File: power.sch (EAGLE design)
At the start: 36 parts, among them IC1 74HC125D, IC2 7805TV, IC3 7815TV

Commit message: fixed more things that had been bothering me.
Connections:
- net GND: now also U$3.P$3; no longer U$3.P$4
- net N$1: now also U$3.P$2, U$4.P$1, U$5.P$2; no longer D1.A, U$3.P$3
- net N$3: now also D1.A, U$3.P$4; no longer IC3.VI, PV+.MOUNT, R3.1, U$3.P$2
- net N$6: now also IC3.VI, PV+.MOUNT, R3.1; no longer U$4.P$1, U$5.P$2
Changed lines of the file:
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@@
 </busses>
 <nets>
-<net name="N$3" class="0">
-<segment>
-<pinref part="R3" gate="G$1" pin="1"/>
-<wire x1="7.62" y1="43.18" x2="2.54" y2="43.18" width="0.1524" layer="91"/>
-<wire x1="7.62" y1="43.18" x2="7.62" y2="40.64" width="0.1524" layer="91"/>
-<wire x1="7.62" y1="40.64" x2="7.62" y2="33.02" width="0.1524" layer="91"/>
-<wire x1="7.62" y1="33.02" x2="2.54" y2="33.02" width="0.1524" layer="91"/>
-<wire x1="7.62" y1="40.64" x2="22.86" y2="40.64" width="0.1524" layer="91"/>
-<junction x="7.62" y="40.64"/>
-<pinref part="U$3" gate="G$1" pin="P$2"/>
-<wire x1="22.86" y1="40.64" x2="22.86" y2="43.18" width="0.1524" layer="91"/>
-<pinref part="PV+" gate="G$1" pin="MOUNT"/>
-<pinref part="IC3" gate="A1" pin="VI"/>
-<wire x1="-58.42" y1="76.2" x2="-60.96" y2="76.2" width="0.1524" layer="91"/>
-<wire x1="-60.96" y1="76.2" x2="-60.96" y2="50.8" width="0.1524" layer="91"/>
-<wire x1="-60.96" y1="50.8" x2="2.54" y2="50.8" width="0.1524" layer="91"/>
-<wire x1="2.54" y1="50.8" x2="2.54" y2="43.18" width="0.1524" layer="91"/>
-<junction x="2.54" y="43.18"/>
-</segment>
-</net>
 <net name="N$9" class="0">
 <segment>
@@
 </segment>
 </net>
-<net name="N$1" class="0">
-<segment>
-<pinref part="D1" gate="1" pin="A"/>
-<pinref part="U$3" gate="G$1" pin="P$3"/>
-<wire x1="55.88" y1="76.2" x2="12.7" y2="76.2" width="0.1524" layer="91"/>
-<wire x1="12.7" y1="76.2" x2="12.7" y2="60.96" width="0.1524" layer="91"/>
-</segment>
-</net>
 <net name="N$2" class="0">
 <segment>
@@
 </segment>
 </net>
-<net name="N$6" class="0">
-<segment>
-<pinref part="U$5" gate="G$1" pin="P$2"/>
-<wire x1="30.48" y1="55.88" x2="27.94" y2="55.88" width="0.1524" layer="91"/>
-<wire x1="27.94" y1="55.88" x2="27.94" y2="45.72" width="0.1524" layer="91"/>
-<pinref part="U$4" gate="G$1" pin="P$1"/>
-<wire x1="27.94" y1="45.72" x2="30.48" y2="45.72" width="0.1524" layer="91"/>
-<junction x="27.94" y="45.72"/>
-<wire x1="27.94" y1="45.72" x2="27.94" y2="38.1" width="0.1524" layer="91"/>
-<wire x1="27.94" y1="38.1" x2="12.7" y2="38.1" width="0.1524" layer="91"/>
-<pinref part="U$3" gate="G$1" pin="P$1"/>
-<wire x1="12.7" y1="38.1" x2="12.7" y2="43.18" width="0.1524" layer="91"/>
-</segment>
-</net>
 <net name="GND" class="0">
 <segment>
-<wire x1="22.86" y1="73.66" x2="50.8" y2="73.66" width="0.1524" layer="91"/>
+<wire x1="12.7" y1="73.66" x2="50.8" y2="73.66" width="0.1524" layer="91"/>
 <wire x1="50.8" y1="73.66" x2="50.8" y2="55.88" width="0.1524" layer="91"/>
 <wire x1="50.8" y1="55.88" x2="50.8" y2="50.8" width="0.1524" layer="91"/>
@@
 <pinref part="R1" gate="G$1" pin="1"/>
 <wire x1="73.66" y1="50.8" x2="78.74" y2="50.8" width="0.1524" layer="91"/>
-<pinref part="U$3" gate="G$1" pin="P$4"/>
-<wire x1="22.86" y1="73.66" x2="22.86" y2="60.96" width="0.1524" layer="91"/>
 <pinref part="U$5" gate="G$1" pin="P$4"/>
 <wire x1="48.26" y1="55.88" x2="50.8" y2="55.88" width="0.1524" layer="91"/>
@@
 <pinref part="GND1" gate="1" pin="GND"/>
 <junction x="60.96" y="50.8"/>
+<pinref part="U$3" gate="G$1" pin="P$3"/>
+<wire x1="12.7" y1="73.66" x2="12.7" y2="60.96" width="0.1524" layer="91"/>
 </segment>
 <segment>
@@
 </segment>
 </net>
+<net name="N$1" class="0">
+<segment>
+<pinref part="U$4" gate="G$1" pin="P$1"/>
+<pinref part="U$5" gate="G$1" pin="P$2"/>
+<wire x1="30.48" y1="55.88" x2="27.94" y2="55.88" width="0.1524" layer="91"/>
+<wire x1="27.94" y1="55.88" x2="27.94" y2="45.72" width="0.1524" layer="91"/>
+<wire x1="27.94" y1="45.72" x2="30.48" y2="45.72" width="0.1524" layer="91"/>
+<junction x="27.94" y="45.72"/>
+<wire x1="27.94" y1="45.72" x2="27.94" y2="38.1" width="0.1524" layer="91"/>
+<wire x1="27.94" y1="38.1" x2="22.86" y2="38.1" width="0.1524" layer="91"/>
+<pinref part="U$3" gate="G$1" pin="P$2"/>
+<wire x1="22.86" y1="43.18" x2="22.86" y2="38.1" width="0.1524" layer="91"/>
+</segment>
+</net>
+<net name="N$6" class="0">
+<segment>
+<pinref part="U$3" gate="G$1" pin="P$1"/>
+<wire x1="12.7" y1="38.1" x2="12.7" y2="43.18" width="0.1524" layer="91"/>
+<pinref part="R3" gate="G$1" pin="1"/>
+<wire x1="7.62" y1="43.18" x2="2.54" y2="43.18" width="0.1524" layer="91"/>
+<wire x1="7.62" y1="43.18" x2="7.62" y2="38.1" width="0.1524" layer="91"/>
+<wire x1="7.62" y1="38.1" x2="7.62" y2="33.02" width="0.1524" layer="91"/>
+<wire x1="7.62" y1="33.02" x2="2.54" y2="33.02" width="0.1524" layer="91"/>
+<pinref part="PV+" gate="G$1" pin="MOUNT"/>
+<pinref part="IC3" gate="A1" pin="VI"/>
+<wire x1="-58.42" y1="76.2" x2="-60.96" y2="76.2" width="0.1524" layer="91"/>
+<wire x1="-60.96" y1="76.2" x2="-60.96" y2="50.8" width="0.1524" layer="91"/>
+<wire x1="-60.96" y1="50.8" x2="2.54" y2="50.8" width="0.1524" layer="91"/>
+<wire x1="2.54" y1="50.8" x2="2.54" y2="43.18" width="0.1524" layer="91"/>
+<junction x="2.54" y="43.18"/>
+<wire x1="12.7" y1="38.1" x2="7.62" y2="38.1" width="0.1524" layer="91"/>
+<junction x="7.62" y="38.1"/>
+</segment>
+</net>
+<net name="N$3" class="0">
+<segment>
+<pinref part="D1" gate="1" pin="A"/>
+<wire x1="55.88" y1="76.2" x2="22.86" y2="76.2" width="0.1524" layer="91"/>
+<pinref part="U$3" gate="G$1" pin="P$4"/>
+<wire x1="22.86" y1="60.96" x2="22.86" y2="76.2" width="0.1524" layer="91"/>
+</segment>
+</net>

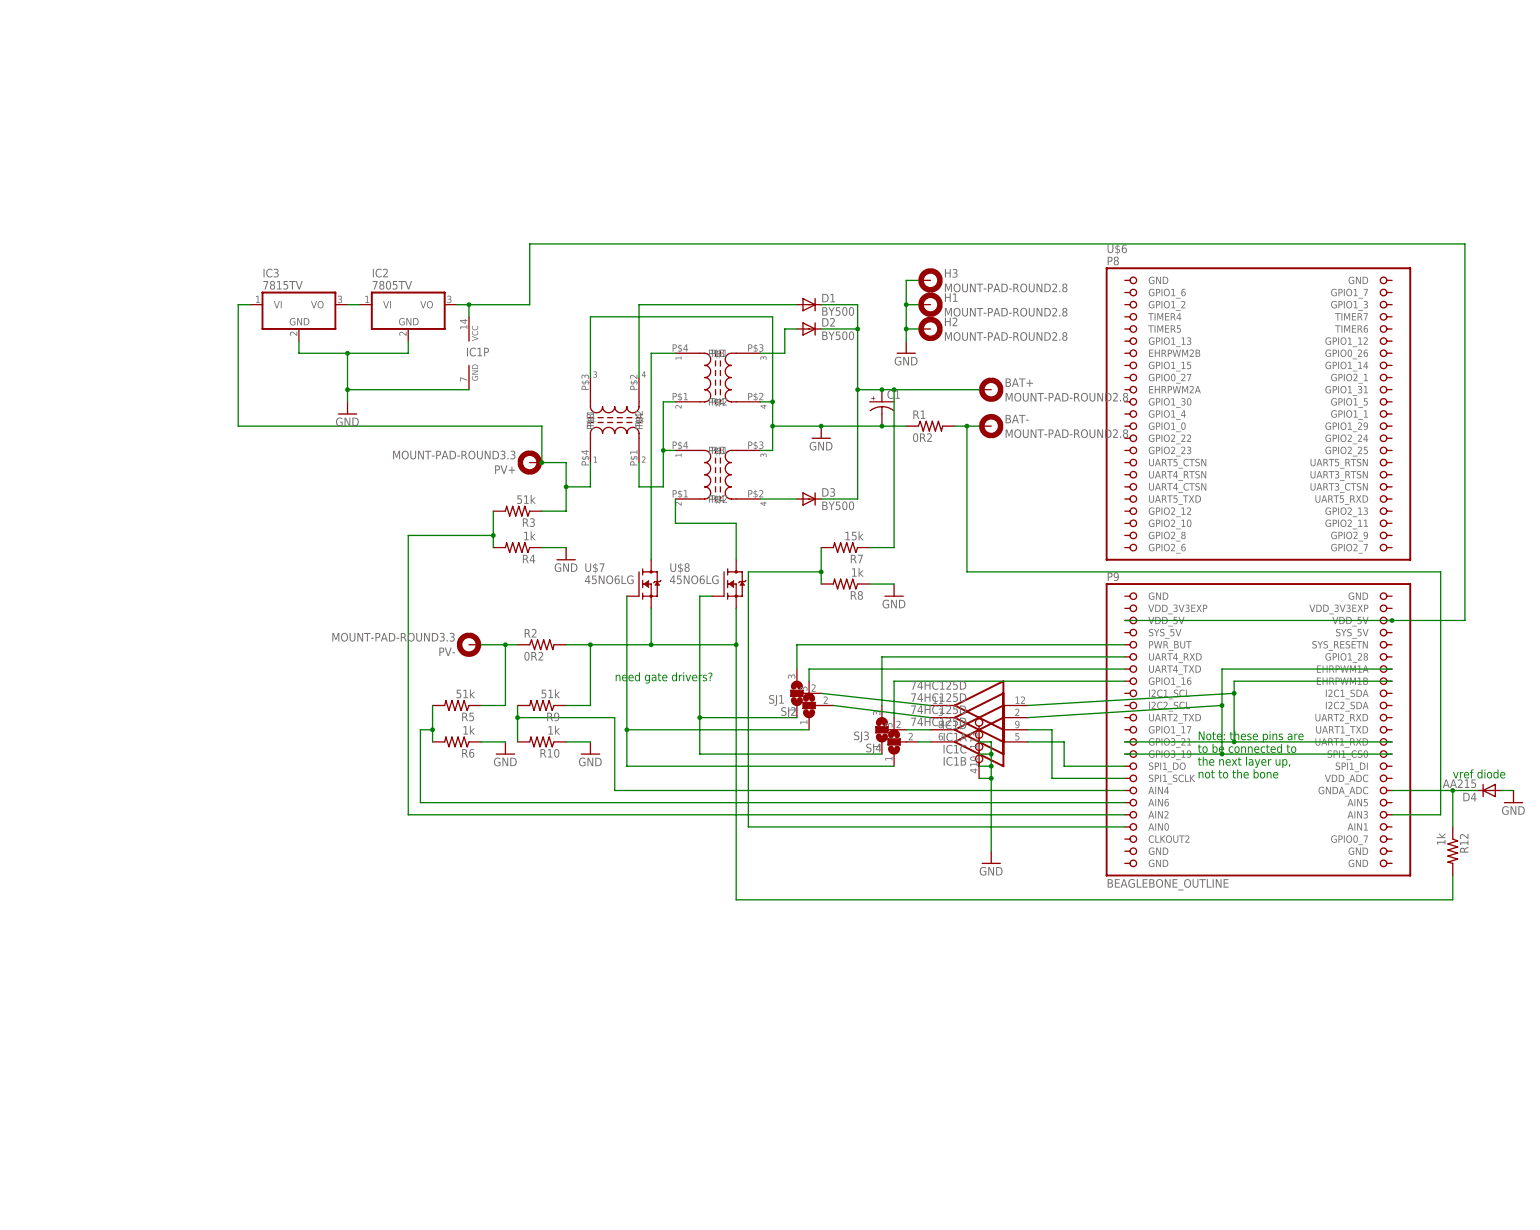
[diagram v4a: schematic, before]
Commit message: Schematic cleanup
Thanks, Roger!
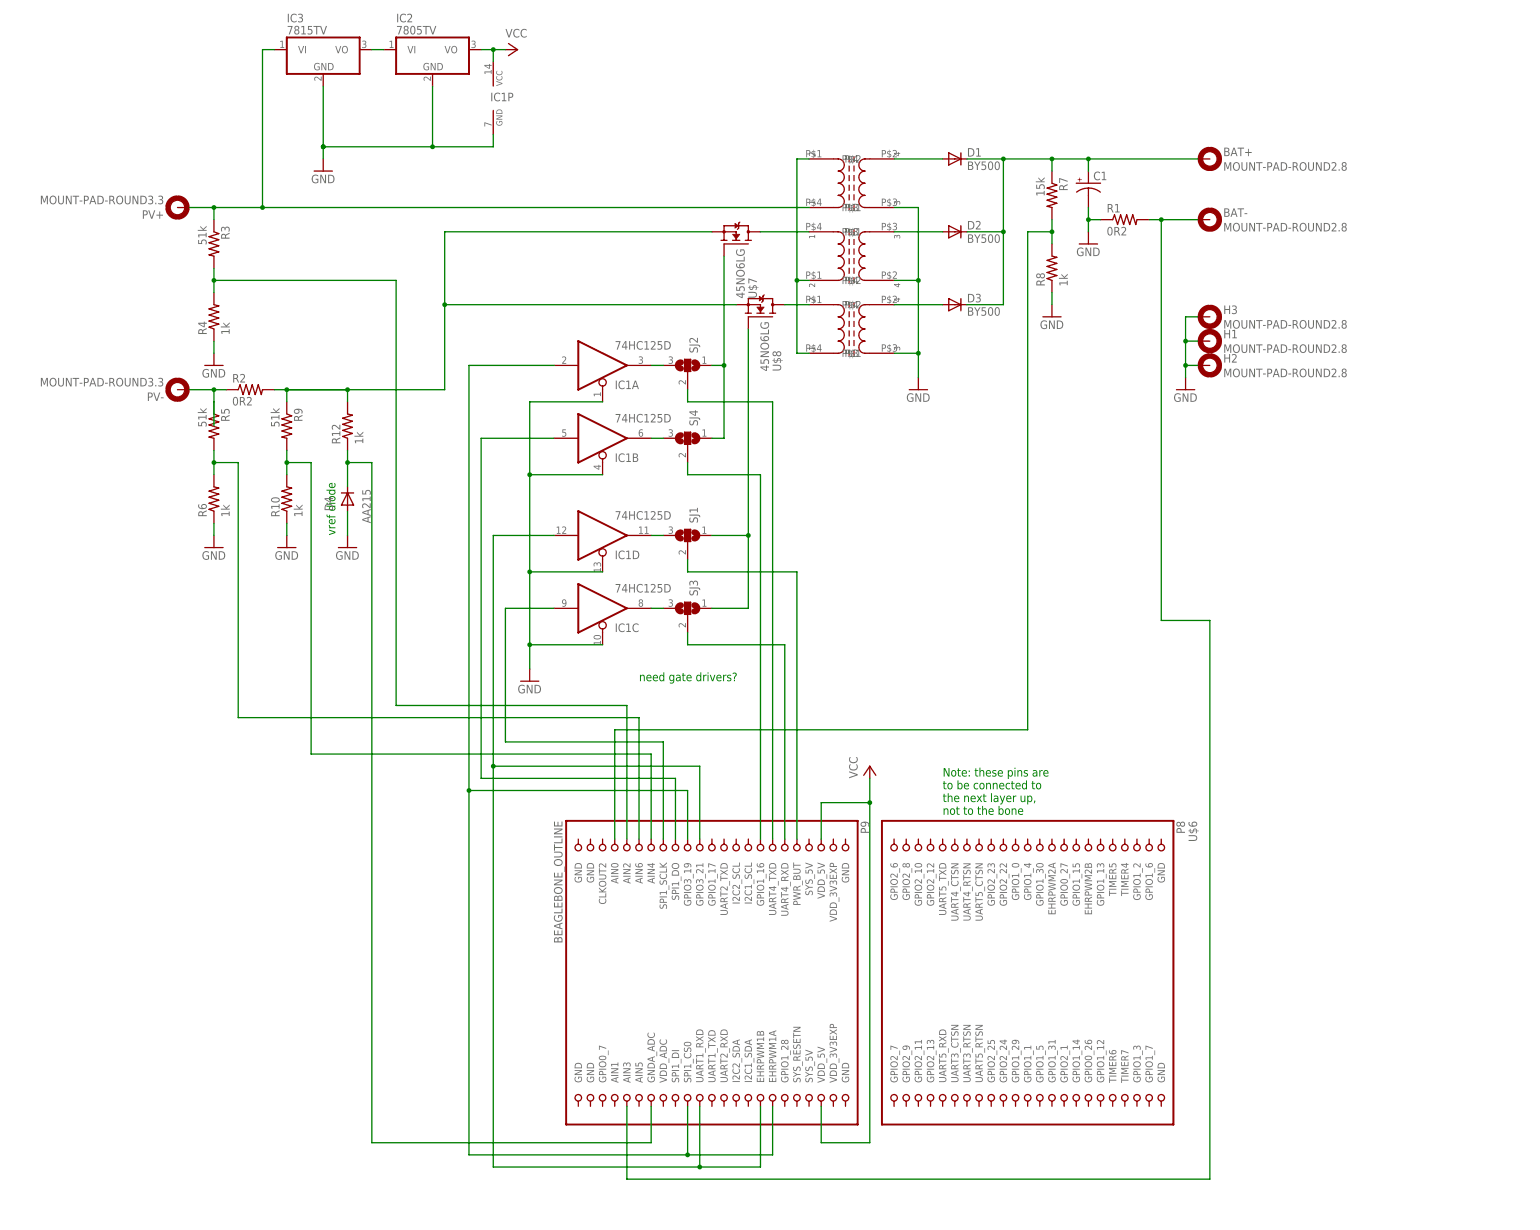
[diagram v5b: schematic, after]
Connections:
- net N$26 renamed VCC
- removed net N$29: IC1C.O, SJ3.2
- removed net N$31: SJ4.3, U$6.GPIO1_16
- removed net N$32: SJ3.3, U$6.UART4_RXD
- removed net N$34: SJ1.3, U$6.PWR_BUT
- removed net N$35: IC1D.O, SJ1.2
- removed net N$36: IC1A.O, SJ2.2
- new net N$19: IC1A.O, SJ2.3
- new net N$20: IC1B.O, SJ4.3
- new net N$21: SJ3.2, U$6.UART4_RXD
- new net N$22: SJ1.2, U$6.PWR_BUT
- new net N$24: IC1D.O, SJ1.3
- new net N$25: IC1C.O, SJ3.3
- net N$30: now also U$6.GPIO1_16; no longer IC1B.O
- net N$33: now also SJ2.2; no longer SJ2.3
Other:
- moved on the sheet: BAT+, BAT-, C1, D1, D2, D3, D4, H1, H2, H3, IC1A, IC1B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

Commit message: Fixed the schematic, rerouted the board
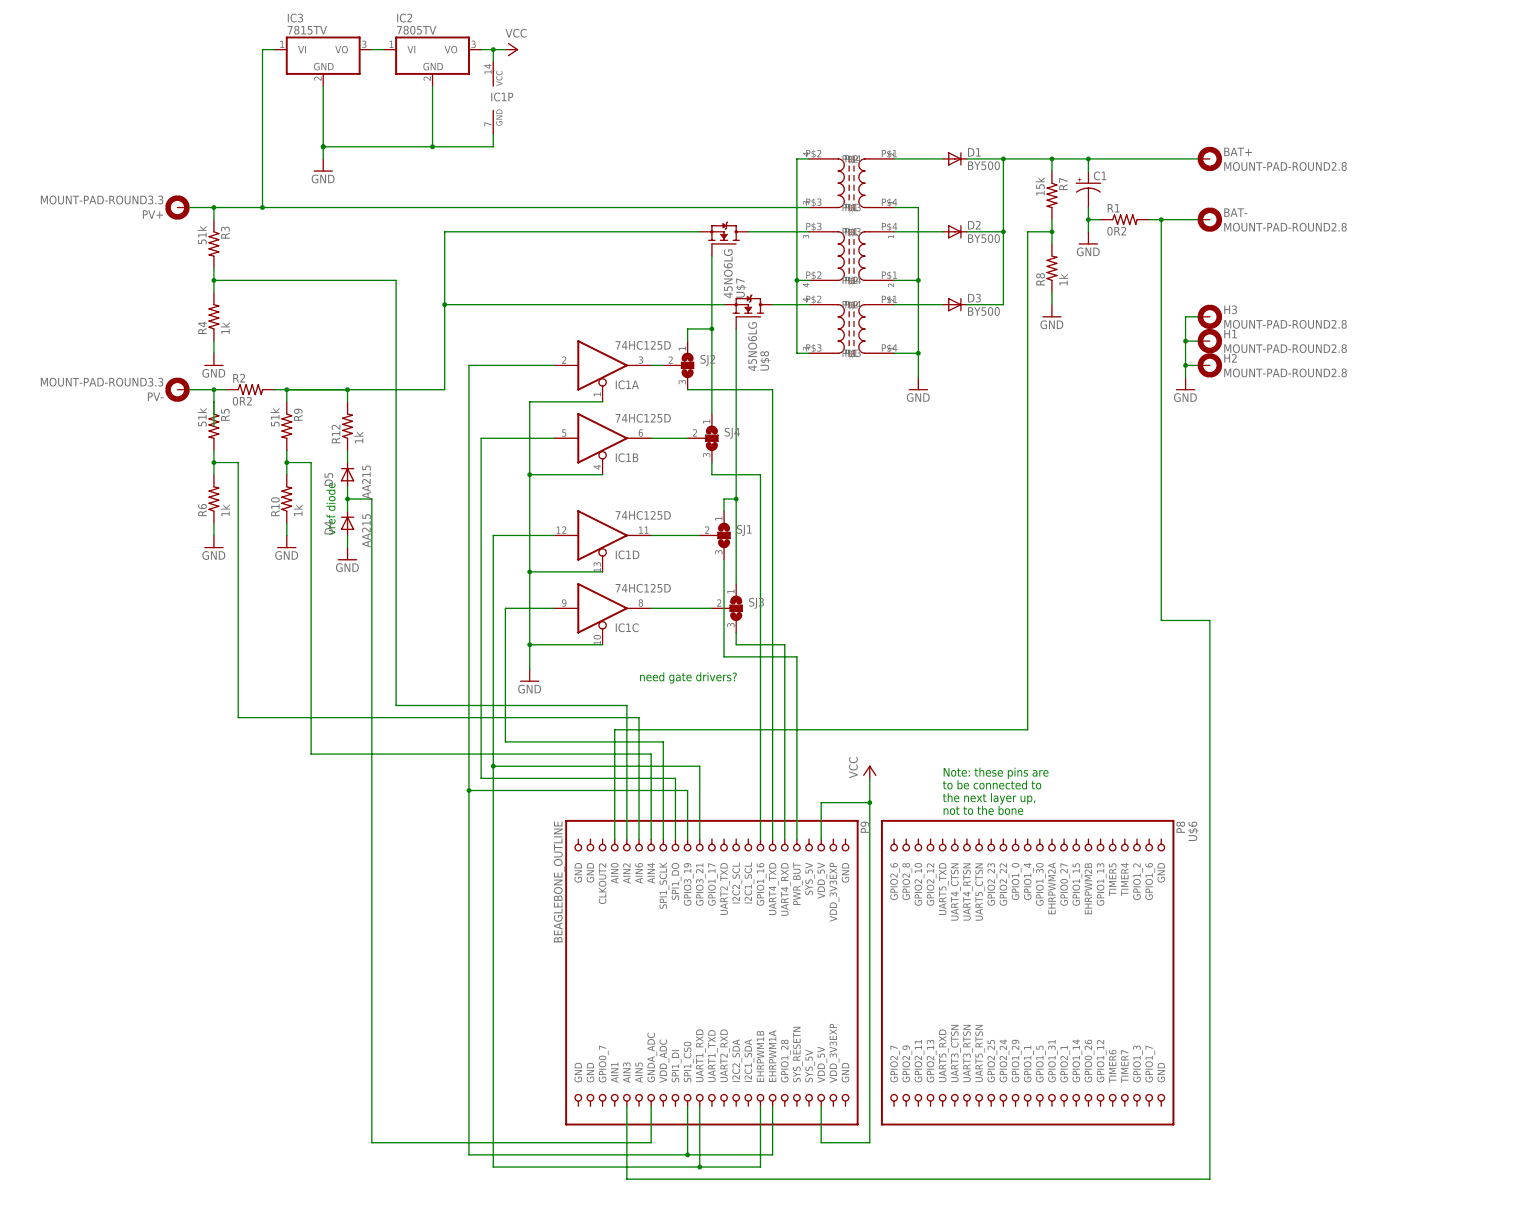
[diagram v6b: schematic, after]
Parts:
- added D5: AA215, diode:AA215
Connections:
- removed net N$30: SJ4.2, U$6.GPIO1_16
- new net N$26: D5.C, R12.1
- new net N$29: IC1C.O, SJ3.2
- net GND: now also U$3.P$1, U$4.P$1, U$5.P$2; no longer U$3.P$3, U$4.P$3, U$5.P$4
- net N$1: now also U$3.P$4, U$4.P$3, U$5.P$4; no longer U$3.P$2, U$4.P$1, U$5.P$2
- net N$14: now also D5.A; no longer R12.1
- net N$15: now also D1.A, U$3.P$2; no longer U$5.P$1, U$7.D
- net N$19: now also SJ1.3, U$6.PWR_BUT; no longer IC1A.O, SJ2.3
- net N$2: now also U$4.P$4, U$8.D; no longer D2.A, U$5.P$3
- net N$20: now also IC1A.O, SJ2.2; no longer IC1B.O, SJ4.3
- net N$21: now also SJ3.3; no longer SJ3.2
- net N$22: now also SJ4.3, U$6.GPIO1_16; no longer SJ1.2, U$6.PWR_BUT
- net N$24: now also IC1B.O, SJ4.2; no longer IC1D.O, SJ1.3
- net N$25: now also IC1D.O, SJ1.2; no longer IC1C.O, SJ3.3
- net N$3: now also U$5.P$3, U$7.D; no longer D1.A, U$3.P$4
- net N$33: now also SJ2.3; no longer SJ2.2
- net N$5: now also D3.A; no longer U$8.D
- net N$6: now also U$3.P$3; no longer U$3.P$1
- net N$9: now also D2.A, U$5.P$1; no longer D3.A, U$4.P$4
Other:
- moved on the sheet: D4, SJ1, SJ2, SJ3, SJ4, U$7, U$8
